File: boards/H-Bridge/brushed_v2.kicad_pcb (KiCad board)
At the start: 4 copper layers, 62 parts, among them IC1 ISO1042QDWVQ1, IC2 MIC4606-1YML-TR, IC3 AD8410AWBRZ-RL, IC4 TC1108-3.3VDBTR, J1 V+, J2 V-, J3 Motor-, J4 Motor+, J5 CANBus, J6 Encoder, J7 Prog_Header, J8 UART, J9 12V+, Q1 NTBLS4D0N15MC, Q2 NTBLS4D0N15MC, Q3 NTBLS4D0N15MC, Q4 NTBLS4D0N15MC, U1 STM32F103C8Tx, U2 LSF0102DCUR, U3 LSF0102DCUR

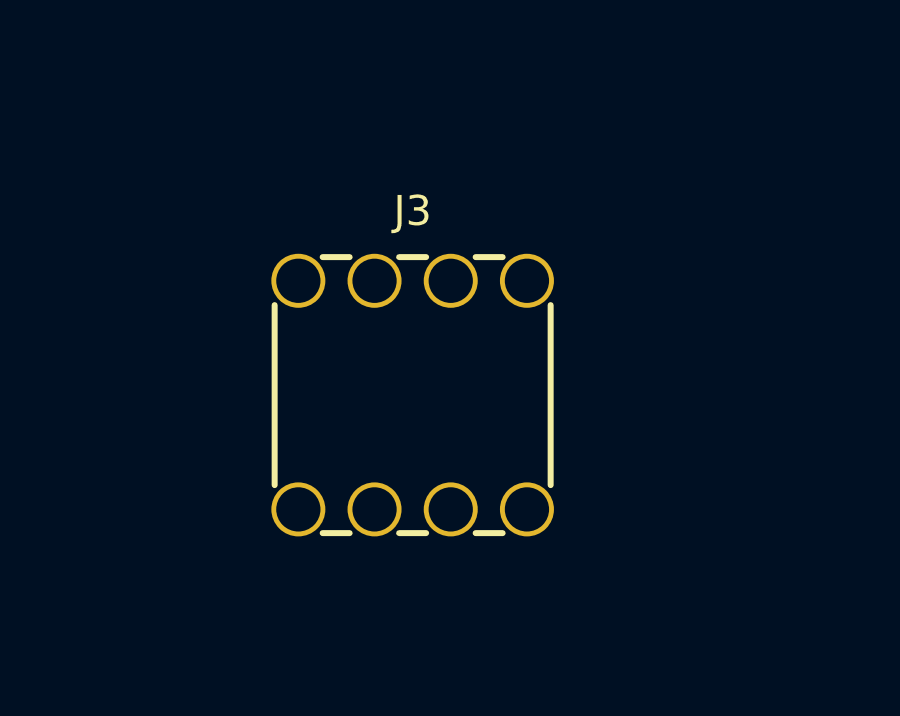
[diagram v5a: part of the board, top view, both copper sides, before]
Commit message: rotated components
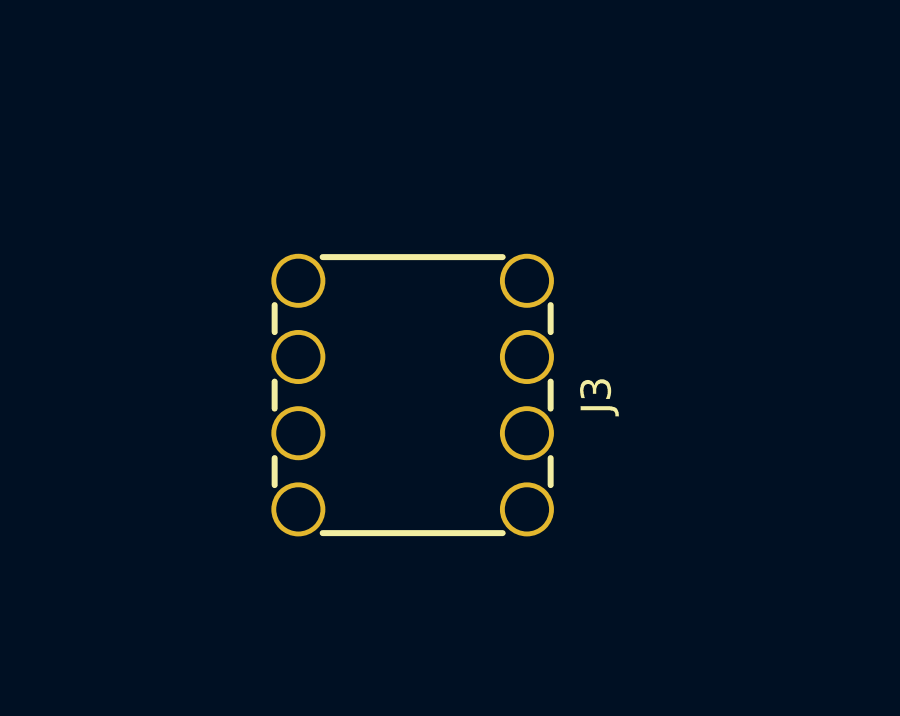
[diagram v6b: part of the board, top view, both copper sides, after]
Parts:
- turned J3 to -90 degrees
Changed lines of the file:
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@@
 		(capping no)
 		(filling no)
-		(zone_defaults)
 		(pcbplotparams
 			(layerselection 0x00000000_00000000_55555555_5755f5ff)
@@
 	(footprint "ThreadedConnector:WP-BUTR_7460307"
 		(layer "F.Cu")
-		(at 228 99)
+		(at 228 99 -90)
 		(property "Reference" "J3"
-			(at 0 -6.135 0)
+			(at 0 -6.135 90)
 			(layer "F.SilkS")
 			(effects
@@
 		)
 		(property "Value" "Motor-"
-			(at 6.025 6.365 0)
+			(at 6.025 6.365 90)
 			(layer "F.Fab")
 			(effects
@@
 		)
 		(property "Datasheet" ""
-			(at 0 0 0)
+			(at 0 0 90)
 			(layer "F.Fab")
 			(hide yes)
@@
 		)
 		(property "Description" "Generic screw terminal, single row, 01x01, script generated (kicad-library-utils/schlib/autogen/connector/)"
-			(at 0 0 0)
+			(at 0 0 90)
 			(layer "F.Fab")
 			(hide yes)
@@
 		(duplicate_pad_numbers_are_jumpers no)
 		(fp_line
-			(start -4.6 3)
-			(end -4.6 -3)
+			(start -2.1 4.6)
+			(end -3 4.6)
 			(stroke
 				(width 0.2)
@@
 		)
 		(fp_line
-			(start -3 -4.6)
-			(end -2.1 -4.6)
+			(start 0.45 4.6)
+			(end -0.45 4.6)
 			(stroke
 				(width 0.2)
@@
 		)
 		(fp_line
-			(start -2.1 4.6)
-			(end -3 4.6)
+			(start 3 4.6)
+			(end 2.1 4.6)
 			(stroke
 				(width 0.2)
@@
 		)
 		(fp_line
-			(start -0.45 -4.6)
-			(end 0.45 -4.6)
+			(start -4.6 3)
+			(end -4.6 -3)
 			(stroke
 				(width 0.2)
@@
 		)
 		(fp_line
-			(start 0.45 4.6)
-			(end -0.45 4.6)
+			(start 4.6 -3)
+			(end 4.6 3)
 			(stroke
 				(width 0.2)
@@
 		)
 		(fp_line
-			(start 2.1 -4.6)
-			(end 3 -4.6)
+			(start -3 -4.6)
+			(end -2.1 -4.6)
 			(stroke
 				(width 0.2)
@@
 		)
 		(fp_line
-			(start 3 4.6)
-			(end 2.1 4.6)
+			(start -0.45 -4.6)
+			(end 0.45 -4.6)
 			(stroke
 				(width 0.2)
@@
 		)
 		(fp_line
-			(start 4.6 -3)
-			(end 4.6 3)
+			(start 2.1 -4.6)
+			(end 3 -4.6)
 			(stroke
 				(width 0.2)
@@
 		)
 		(fp_line
-			(start -4.5 -4.5)
-			(end 4.5 -4.5)
+			(start -4.5 4.5)
+			(end -4.5 -4.5)
 			(stroke
 				(width 0.1)
@@
 		)
 		(fp_line
-			(start -4.5 4.5)
-			(end -4.5 -4.5)
+			(start 4.5 4.5)
+			(end -4.5 4.5)
 			(stroke
 				(width 0.1)
@@
 		)
 		(fp_line
-			(start 4.5 -4.5)
-			(end 4.5 4.5)
+			(start -4.5 -4.5)
+			(end 4.5 -4.5)
 			(stroke
 				(width 0.1)
@@
 		)
 		(fp_line
-			(start 4.5 4.5)
-			(end -4.5 4.5)
+			(start 4.5 -4.5)
+			(end 4.5 4.5)
 			(stroke
 				(width 0.1)
@@
 		)
 		(pad "1" thru_hole circle
-			(at -3.81 -3.81)
+			(at -3.81 -3.81 270)
 			(size 1.8 1.8)
 			(drill 1.475)
@@
 		)
 		(pad "1" thru_hole circle
-			(at -3.81 3.81)
+			(at -3.81 3.81 270)
 			(size 1.8 1.8)
 			(drill 1.475)
@@
 		)
 		(pad "1" thru_hole circle
-			(at -1.27 -3.81)
+			(at -1.27 -3.81 270)
 			(size 1.8 1.8)
 			(drill 1.475)
@@
 		)
 		(pad "1" thru_hole circle
-			(at -1.27 3.81)
+			(at -1.27 3.81 270)
 			(size 1.8 1.8)
 			(drill 1.475)
@@
 		)
 		(pad "1" thru_hole circle
-			(at 1.27 -3.81)
+			(at 1.27 -3.81 270)
 			(size 1.8 1.8)
 			(drill 1.475)
@@
 		)
 		(pad "1" thru_hole circle
-			(at 1.27 3.81)
+			(at 1.27 3.81 270)
 			(size 1.8 1.8)
 			(drill 1.475)
@@
 		)
 		(pad "1" thru_hole circle
-			(at 3.81 -3.81)
+			(at 3.81 -3.81 270)
 			(size 1.8 1.8)
 			(drill 1.475)
@@
 		)
 		(pad "1" thru_hole circle
-			(at 3.81 3.81)
+			(at 3.81 3.81 270)
 			(size 1.8 1.8)
 			(drill 1.475)

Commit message: FET layout nearing completion
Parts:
- moved C5 116.7 mm to (180.8, 140.5), turned to 180 degrees
- moved C6 89.5 mm to (179.9, 81.2), turned to 180 degrees
- moved IC3 32.1 mm to (185.5, 122.8), turned to -90 degrees
- moved J4 31.6 mm to (196.8, 112.5)
- moved J3 31.3 mm to (196.8, 98.8)
- moved R5 21.6 mm to (182.0, 89.2)
- moved Q1 19.9 mm to (190.1, 135.7), turned to 180 degrees
- moved R1 19.4 mm to (196.8, 123.0), turned to 90 degrees
- moved Q3 18.0 mm to (190.2, 83.3), turned to 0 degrees
- moved R8 14.0 mm to (181.3, 132.5)
- moved Q4 13.0 mm to (204.8, 83.0)
- moved R6 12.0 mm to (197.5, 81.5), turned to 90 degrees
- moved R7 10.8 mm to (197.2, 139.0), turned to 90 degrees
- moved Q2 8.42 mm to (204.4, 135.7)
- moved R13 3.09 mm to (178.0, 103.8)
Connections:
- J4 pad 1: /High Voltage&Sense/SHUNT+ -> /High Voltage&Sense/SHUNT-
- Q1 pad 1: /High Voltage&Sense/SHUNT- -> /High Voltage&Sense/SHUNT+
- Q1 pad 2: /High Voltage&Sense/SHUNT- -> /High Voltage&Sense/SHUNT+
- Q1 pad 3: /High Voltage&Sense/SHUNT- -> /High Voltage&Sense/SHUNT+
- Q1 pad 4: /High Voltage&Sense/SHUNT- -> /High Voltage&Sense/SHUNT+
- Q1 pad 5: /High Voltage&Sense/SHUNT- -> /High Voltage&Sense/SHUNT+
- Q1 pad 6: /High Voltage&Sense/SHUNT- -> /High Voltage&Sense/SHUNT+
- Q1 pad 7: /High Voltage&Sense/SHUNT- -> /High Voltage&Sense/SHUNT+
- Q2 pad 10: /High Voltage&Sense/SHUNT- -> /High Voltage&Sense/SHUNT+
- Q2 pad 11: /High Voltage&Sense/SHUNT- -> /High Voltage&Sense/SHUNT+
- Q2 pad 12: /High Voltage&Sense/SHUNT- -> /High Voltage&Sense/SHUNT+
- Q2 pad 13: /High Voltage&Sense/SHUNT- -> /High Voltage&Sense/SHUNT+
- Q2 pad 9: /High Voltage&Sense/SHUNT- -> /High Voltage&Sense/SHUNT+
- R1 pad 1: /High Voltage&Sense/SHUNT- -> /High Voltage&Sense/SHUNT+
- R1 pad 2: /High Voltage&Sense/SHUNT+ -> /High Voltage&Sense/SHUNT-
- R12 pad 1: /High Voltage&Sense/SHUNT- -> /High Voltage&Sense/SHUNT+
- U1 pad 26: /MCU&Low_Voltage/CHA_3.3 -> unconnected-(U1-PB13-Pad26)
- U1 pad 27: /MCU&Low_Voltage/CHB_3.3 -> unconnected-(U1-PB14-Pad27)
- U1 pad 42: unconnected-(U1-PB6-Pad42) -> /MCU&Low_Voltage/CHA_3.3
- U1 pad 43: unconnected-(U1-PB7-Pad43) -> /MCU&Low_Voltage/CHB_3.3
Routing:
- net Net-(IC2-ALO): track 0.00 -> 16.4 mm
- net /High Voltage&Sense/GATEA_HIGH: track 0.00 -> 13.9 mm
- net /High Voltage&Sense/SHUNT+: track 0.00 -> 12.9 mm
- net /High Voltage&Sense/SHUNT-: track 0.00 -> 12.8 mm

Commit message: moved components to better current sense
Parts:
- moved R12 8.55 mm to (173.5, 123.5), turned to 90 degrees
- moved IC3 5.52 mm to (180.0, 123.2)
- moved D3 2.61 mm to (170.0, 118.2), turned to 180 degrees
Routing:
- net /High Voltage&Sense/SHUNT+: track 12.9 -> 0.00 mm
- net /High Voltage&Sense/SHUNT-: track 12.8 -> 0.00 mm
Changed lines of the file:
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@@
 	(footprint "Diode_SMD:D_SMA"
 		(layer "F.Cu")
-		(at 172.5 119 -90)
+		(at 170 118.25 180)
 		(descr "Diode SMA (DO-214AC)")
 		(tags "Diode SMA (DO-214AC)")
 		(property "Reference" "D3"
-			(at 0 -2.5 90)
+			(at 0 -2.5 0)
 			(layer "F.SilkS")
 			(effects
@@
 		)
 		(property "Value" "SS1200"
-			(at 0 2.6 90)
+			(at 0 2.6 0)
 			(layer "F.Fab")
 			(effects
@@
 		)
 		(property "Datasheet" "https://www.wontop.com/uploadfiles/56/sort_excel/pdf/ss1150.pdf"
-			(at 0 0 270)
+			(at 0 0 180)
 			(unlocked yes)
 			(layer "F.Fab")
@@
 		)
 		(property "Description" "200V 1A Schottky Diode, SMA"
-			(at 0 0 270)
+			(at 0 0 180)
 			(unlocked yes)
 			(layer "F.Fab")
@@
 		(fp_line
 			(start -3.51 -1.65)
-			(end -3.51 1.65)
+			(end 2 -1.65)
 			(stroke
 				(width 0.12)
@@
 		(fp_line
 			(start -3.51 -1.65)
-			(end 2 -1.65)
+			(end -3.51 1.65)
 			(stroke
 				(width 0.12)
@@
 		)
 		(fp_line
-			(start -3.5 1.75)
-			(end -3.5 -1.75)
+			(start 3.5 1.75)
+			(end -3.5 1.75)
 			(stroke
 				(width 0.05)
@@
 		)
 		(fp_line
-			(start 3.5 1.75)
-			(end -3.5 1.75)
+			(start 3.5 -1.75)
+			(end 3.5 1.75)
 			(stroke
 				(width 0.05)
@@
 		)
 		(fp_line
-			(start -3.5 -1.75)
-			(end 3.5 -1.75)
+			(start -3.5 1.75)
+			(end -3.5 -1.75)
 			(stroke
 				(width 0.05)
@@
 		)
 		(fp_line
-			(start 3.5 -1.75)
-			(end 3.5 1.75)
+			(start -3.5 -1.75)
+			(end 3.5 -1.75)
 			(stroke
 				(width 0.05)
@@
 		)
 		(fp_line
-			(start -2.3 1.5)
-			(end -2.3 -1.5)
+			(start 2.3 1.5)
+			(end -2.3 1.5)
 			(stroke
 				(width 0.1)
@@
 		)
 		(fp_line
-			(start 2.3 1.5)
-			(end -2.3 1.5)
+			(start 2.3 -1.5)
+			(end 2.3 1.5)
 			(stroke
 				(width 0.1)
@@
 		)
 		(fp_line
-			(start 0.50118 0.75032)
-			(end 0.50118 -0.79908)
+			(start 2.3 -1.5)
+			(end -2.3 -1.5)
 			(stroke
 				(width 0.1)
@@
 		)
 		(fp_line
-			(start -0.64944 0.00102)
-			(end 0.50118 0.75032)
+			(start 0.50118 0.75032)
+			(end 0.50118 -0.79908)
 			(stroke
 				(width 0.1)
@@
 		)
 		(fp_line
-			(start -0.64944 0.00102)
-			(end -1.55114 0.00102)
+			(start 0.50118 0.00102)
+			(end 1.4994 0.00102)
 			(stroke
 				(width 0.1)
@@
 		(fp_line
 			(start -0.64944 0.00102)
-			(end 0.50118 -0.79908)
+			(end 0.50118 0.75032)
 			(stroke
 				(width 0.1)
@@
 		)
 		(fp_line
-			(start 0.50118 0.00102)
-			(end 1.4994 0.00102)
+			(start -0.64944 0.00102)
+			(end 0.50118 -0.79908)
 			(stroke
 				(width 0.1)
@@
 		)
 		(fp_line
-			(start -0.64944 -0.79908)
-			(end -0.64944 0.80112)
+			(start -0.64944 0.00102)
+			(end -1.55114 0.00102)
 			(stroke
 				(width 0.1)
@@
 		)
 		(fp_line
-			(start 2.3 -1.5)
-			(end 2.3 1.5)
+			(start -0.64944 -0.79908)
+			(end -0.64944 0.80112)
 			(stroke
 				(width 0.1)
@@
 		)
 		(fp_line
-			(start 2.3 -1.5)
+			(start -2.3 1.5)
 			(end -2.3 -1.5)
 			(stroke
@@
 		)
 		(fp_text user "${REFERENCE}"
-			(at 0 -2.5 90)
+			(at 0 -2.5 0)
 			(layer "F.Fab")
 			(effects
@@
 		)
 		(pad "1" smd roundrect
-			(at -2 0 270)
+			(at -2 0 180)
 			(size 2.5 1.8)
 			(layers "F.Cu" "F.Mask" "F.Paste")
@@
 		)
 		(pad "2" smd roundrect
-			(at 2 0 270)
+			(at 2 0 180)
 			(size 2.5 1.8)
 			(layers "F.Cu" "F.Mask" "F.Paste")
@@
 	(footprint "Package_SO:MSOP-8_3x3mm_P0.65mm"
 		(layer "F.Cu")
-		(at 185.5 122.825 -90)
+		(at 180 123.25 -90)
 		(descr "MSOP, 8 Pin (https://www.jedec.org/system/files/docs/mo-187F.pdf variant AA)")
 		(tags "MSOP SO")
@@
 	(footprint "Resistor_SMD:R_0603_1608Metric"
 		(layer "F.Cu")
-		(at 178.75 116.75 180)
+		(at 173.5 123.5 90)
 		(descr "Resistor SMD 0603 (1608 Metric), square (rectangular) end terminal, IPC-7351 nominal, (Body size source: IPC-SM-782 page 72, https://www.pcb-3d.com/wordpress/wp-content/uploads/ipc-sm-782a_amendment_1_and_2.pdf)")
 		(tags "resistor")
 		(property "Reference" "R12"
-			(at 0 -1.43 0)
+			(at 0 -1.43 90)
 			(layer "F.SilkS")
 			(effects
@@
 		)
 		(property "Value" "3"
-			(at 0 1.43 0)
+			(at 0 1.43 90)
 			(layer "F.Fab")
 			(effects
@@
 		)
 		(property "Datasheet" ""
-			(at 0 0 0)
+			(at 0 0 90)
 			(layer "F.Fab")
 			(hide yes)
@@
 		)
 		(property "Description" "Resistor, US symbol"
-			(at 0 0 0)
+			(at 0 0 90)
 			(layer "F.Fab")
 			(hide yes)
@@
 		)
 		(property "KiLib_Generator" "SMD_2terminal_chip_molded"
-			(at 0 0 0)
+			(at 0 0 90)
 			(layer "F.SilkS")
 			(hide yes)
@@
 		(duplicate_pad_numbers_are_jumpers no)
 		(fp_line
-			(start -0.237258 0.5225)
-			(end 0.237258 0.5225)
+			(start -0.237258 -0.5225)
+			(end 0.237258 -0.5225)
 			(stroke
 				(width 0.12)
@@
 		)
 		(fp_line
-			(start -0.237258 -0.5225)
-			(end 0.237258 -0.5225)
+			(start -0.237258 0.5225)
+			(end 0.237258 0.5225)
 			(stroke
 				(width 0.12)
@@
 		)
 		(fp_text user "${REFERENCE}"
-			(at 0 0 0)
+			(at 0 0 90)
 			(layer "F.Fab")
 			(effects
@@
 		)
 		(pad "1" smd roundrect
-			(at -0.825 0 180)
+			(at -0.825 0 90)
 			(size 0.8 0.95)
 			(layers "F.Cu" "F.Mask" "F.Paste")
@@
 		)
 		(pad "2" smd roundrect
-			(at 0.825 0 180)
+			(at 0.825 0 90)
 			(size 0.8 0.95)
 			(layers "F.Cu" "F.Mask" "F.Paste")
@@
 	)
 	(segment
-		(start 187 122)
-		(end 186.475 121.475)
-		(width 0.2)
-		(layer "F.Cu")
-		(net "/High Voltage&Sense/SHUNT-")
-	)
-	(segment
-		(start 196.75 121.25)
-		(end 196 122)
-		(width 0.2)
-		(layer "F.Cu")
-		(net "/High Voltage&Sense/SHUNT-")
-	)
-	(segment
-		(start 186.475 121.475)
-		(end 186.475 120.7125)
-		(width 0.2)
-		(layer "F.Cu")
-		(net "/High Voltage&Sense/SHUNT-")
-	)
-	(segment
-		(start 196.75 120.0375)
-		(end 196.75 121.25)
-		(width 0.2)
-		(layer "F.Cu")
-		(net "/High Voltage&Sense/SHUNT-")
-	)
-	(segment
-		(start 196 122)
-		(end 187 122)
-		(width 0.2)
-		(layer "F.Cu")
-		(net "/High Voltage&Sense/SHUNT-")
-	)
-	(segment
-		(start 187 123.75)
-		(end 186.475 124.275)
-		(width 0.2)
-		(layer "F.Cu")
-		(net "/High Voltage&Sense/SHUNT+")
-	)
-	(segment
-		(start 196 123.75)
-		(end 187 123.75)
-		(width 0.2)
-		(layer "F.Cu")
-		(net "/High Voltage&Sense/SHUNT+")
-	)
-	(segment
-		(start 196.75 124.5)
-		(end 196 123.75)
-		(width 0.2)
-		(layer "F.Cu")
-		(net "/High Voltage&Sense/SHUNT+")
-	)
-	(segment
-		(start 186.475 124.275)
-		(end 186.475 124.9375)
-		(width 0.2)
-		(layer "F.Cu")
-		(net "/High Voltage&Sense/SHUNT+")
-	)
-	(segment
-		(start 196.75 125.9625)
-		(end 196.75 124.5)
-		(width 0.2)
-		(layer "F.Cu")
-		(net "/High Voltage&Sense/SHUNT+")
-	)
-	(segment
